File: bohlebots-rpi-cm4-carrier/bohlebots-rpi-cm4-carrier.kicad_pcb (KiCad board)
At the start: 2 copper layers, 28 parts, among them J1 SI-46001-F, J2 power_reference, J3 IO_Conn_02x05, J4 I2C_Conn_1x04, K1 Kicker, T1 Taster_LED, T2 Taster_LED, U1 Compute_Module_4_Connectors, U2 USB_Conn_01x05_Pin, X1 Miromatch

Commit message: Added esd protection TODO: find fitting tvs diode (tht) 2p, 4p
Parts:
- removed C1: 100n, Capacitor_THT:C_Radial_D5.0mm_H11.0mm_P2.00mm
- removed C2: 10u, Capacitor_THT:C_Radial_D5.0mm_H11.0mm_P2.00mm
- removed D1: LED, LED_THT:LED_D5.0mm_FlatTop
- removed D36V28FX1: 5V, bohlebots:D36V28FX
- removed D36V28FX2: 3.3V, bohlebots:D36V28FX
- removed ESCON1, ESCON2, ESCON3, ESCON4: 24_2, bohlebots:ESCOM_24_2
- removed H1: Pinhead_1x04V, bohlebots:PinHeader_1x04_P2.54mm_Vertical
- removed J1: SI-46001-F, SI_46001_F:CONN_46001-F_BEL
- removed J2: power_reference, Connector_PinHeader_2.54mm:PinHeader_1x02_P2.54mm_Vertical
- removed J3: IO_Conn_02x05, Connector_PinHeader_2.54mm:PinHeader_2x06_P2.54mm_Vertical
- removed J4: I2C_Conn_1x04, Connector_PinHeader_2.54mm:PinHeader_1x04_P2.54mm_Vertical
- removed JP1, JP2, JP3, JP4: B8B-PH-K, bohlebots:B8B-PH-K
- removed K1: Kicker, bohlebots:KICKER
- removed R1, R2, R3: 10k, Resistor_THT:R_Axial_DIN0207_L6.3mm_D2.5mm_P7.62mm_Horizontal
- removed R4: 1k, Resistor_THT:R_Axial_DIN0207_L6.3mm_D2.5mm_P7.62mm_Horizontal
- removed T1, T2: Taster_LED, bohlebots:TASTER_LED
- removed U1: Compute_Module_4_Connectors, RPi_Compute_Module_4:Raspberry-Pi-4-Compute-Module
- removed U2: USB_Conn_01x05_Pin, Connector_PinHeader_2.54mm:PinHeader_1x04_P2.54mm_Vertical
- removed X1: Miromatch, bohlebots:MICROMATCH-4

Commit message: Started routing.
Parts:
- added C1: 100n, Capacitor_THT:C_Radial_D5.0mm_H11.0mm_P2.00mm, F.Cu at (99.1, 31.6)
- added C2: 10u, Capacitor_THT:C_Radial_D5.0mm_H11.0mm_P2.00mm, F.Cu at (99.1, 38.1)
- added D1: LED, LED_THT:LED_D5.0mm_FlatTop, F.Cu at (83.8, 53.3)
- added D36V28FX1: 5V, bohlebots:D36V28FX, F.Cu at (238.9, 40.0)
- added D36V28FX2: 3.3V, bohlebots:D36V28FX, F.Cu at (259.8, 40.0)
- added ESCON1: 24_2, bohlebots:ESCOM_24_2, F.Cu at (36.6, 87.5)
- added ESCON2: 24_2, bohlebots:ESCOM_24_2, F.Cu at (36.6, 115.3)
- added ESCON3: 24_2, bohlebots:ESCOM_24_2, F.Cu at (36.6, 143.1)
- added ESCON4: 24_2, bohlebots:ESCOM_24_2, F.Cu at (36.6, 170.9)
- added H1: Pinhead_1x04V, bohlebots:PinHeader_1x04_P2.54mm_Vertical, F.Cu at (58.4, 30.3)
- added J1: SI-46001-F, SI_46001_F:CONN_46001-F_BEL, F.Cu at (241.3, 106.7)
- added J2: power_reference, Connector_PinHeader_2.54mm:PinHeader_1x02_P2.54mm_Vertical, F.Cu at (238.8, 81.3)
- added J3: IO_Conn_02x05, Connector_PinHeader_2.54mm:PinHeader_2x06_P2.54mm_Vertical, F.Cu at (251.5, 78.7)
- added J4: I2C_Conn_1x04, Connector_PinHeader_2.54mm:PinHeader_1x04_P2.54mm_Vertical, F.Cu at (63.5, 30.3)
- added JP1: B8B-PH-K, bohlebots:B8B-PH-K, F.Cu at (103.7, 154.9)
- added JP2: B8B-PH-K, bohlebots:B8B-PH-K, F.Cu at (124.9, 154.9)
- added JP3: B8B-PH-K, bohlebots:B8B-PH-K, F.Cu at (103.7, 165.1)
- added JP4: B8B-PH-K, bohlebots:B8B-PH-K, F.Cu at (124.5, 165.1)
- added K1: Kicker, bohlebots:KICKER, F.Cu at (63.5, 182.9)
- added R1: 10k, Resistor_THT:R_Axial_DIN0207_L6.3mm_D2.5mm_P7.62mm_Horizontal, F.Cu at (80.7, 27.9)
- added R2: 10k, Resistor_THT:R_Axial_DIN0207_L6.3mm_D2.5mm_P7.62mm_Horizontal, F.Cu at (80.7, 31.9)
- added R3: 10k, Resistor_THT:R_Axial_DIN0207_L6.3mm_D2.5mm_P7.62mm_Horizontal, F.Cu at (80.7, 36.0)
- added R4: 1k, Resistor_THT:R_Axial_DIN0207_L6.3mm_D2.5mm_P7.62mm_Horizontal, F.Cu at (80.7, 40.0)
- added T1: Taster_LED, bohlebots:TASTER_LED, F.Cu at (35.5, 36.2)
- added T2: Taster_LED, bohlebots:TASTER_LED, F.Cu at (35.6, 55.9)
- added U1: Compute_Module_4_Connectors, RPi_Compute_Module_4:Raspberry-Pi-4-Compute-Module, F.Cu at (138.0, 71.6)
- added U2: USB_Conn_01x05_Pin, Connector_PinHeader_2.54mm:PinHeader_1x04_P2.54mm_Vertical, F.Cu at (68.6, 30.3)
- added U3: DT1446-04SO-7, bohlebots-rpi-cm4-carrier:SOT26, F.Cu at (65.1, 49.6)
- added U5: DT1446-04SO-7, bohlebots-rpi-cm4-carrier:SOT26, F.Cu at (63.5, 58.4)
- added X1: Miromatch, bohlebots:MICROMATCH-4, F.Cu at (109.2, 27.9)

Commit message: PCB Layout Update.
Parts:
- moved J4 199.5 mm to (251.0, -37.8)
- moved R1 199.1 mm to (35.5, 221.8)
- moved R4 186.5 mm to (197.8, 185.2)
- moved T1 175.1 mm to (185.0, -55.0)
- moved R2 171.9 mm to (248.4, -5.80)
- moved R3 171.6 mm to (248.4, -0.74)
- moved U2 171.4 mm to (229.1, 90.4), turned to -90 degrees
- moved J2 169.3 mm to (76.0, 34.5)
- moved D1 168.7 mm to (200.2, 175.5)
- moved U5 164.1 mm to (225.2, 86.5), turned to 90 degrees
- moved T2 160.0 mm to (150.5, -55.5)
- moved U3 148.9 mm to (210.7, 18.6), turned to 180 degrees
- moved X1 148.7 mm to (250.7, -17.8)
- moved D36V28FX1 120.6 mm to (355.5, 70.9)
- moved D36V28FX2 117.0 mm to (355.5, 107.4)
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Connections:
- U5 pad 1: Net-(U5-D1-) -> /USB_N
- U5 pad 3: /USB_P -> Net-(U5-D2-)
- U5 pad 4: /USB_N -> Net-(U5-D2+)

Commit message: Updated pcb layout.
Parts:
- moved D1 251.1 mm to (357.9, -19.9)
- moved R4 251.1 mm to (355.4, -10.3)
- moved J3 225.8 mm to (342.7, -23.5)
- moved U2 128.4 mm to (311.1, -8.42)
- moved U1 128.4 mm to (291.2, -36.9)
- moved U5 128.4 mm to (307.2, -12.4)
- moved C1 128.4 mm to (286.2, -79.7)
- moved J1 128.4 mm to (288.4, -72.8)
- moved U3 128.4 mm to (292.7, -80.2)
- moved H1 118.8 mm to (-60.4, 29.7)
- moved K1 115.9 mm to (-93.1, 217.1)
- moved C2 115.9 mm to (-50.9, 32.4)
- moved ESCON1 115.9 mm to (-79.9, 84.9)
- moved ESCON2 115.9 mm to (-80.0, 113.7)
- moved ESCON3 115.9 mm to (-80.0, 141.5)
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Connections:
- U1 pad 78: unconnected-(U1A-GPIO_VREF-Pad78) -> Net-(U1A-GPIO_VREF)
- U1 pad 84: Net-(U1A-CM4_3.3V_Out-Pad84) -> Net-(U1A-GPIO_VREF)
- U1 pad 86: Net-(U1A-CM4_3.3V_Out-Pad84) -> Net-(U1A-GPIO_VREF)
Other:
- board text added: "Chassie Rand"
- board text added: "Spiegel Zone"

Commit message: IC placement done.
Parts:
- removed H1: Pinhead_1x04V, bohlebots:PinHeader_1x04_P2.54mm_Vertical
- added J5: pwr_connector, Connector_PinHeader_2.54mm:PinHeader_1x03_P2.54mm_Vertical, F.Cu at (48.5, 102.5)
- added J6: pwr_connector, Connector_PinHeader_2.54mm:PinHeader_1x03_P2.54mm_Vertical, F.Cu at (163.5, 107.5)
- added Luxonis OAK-FFP 4P: Luxonis_OAK-FFC-4P_Foothold, bohlebots-rpi-cm4-carrier:Luxonis_OAK-FFC-4P_Foothold, F.Cu at (106.0, 105.0)
- moved D36V28FX2 348.5 mm to (88.5, 117.4)
- moved D36V28FX1 318.7 mm to (118.5, 117.4)
- moved U2 272.0 mm to (65.5, 108.5), turned to 180 degrees
- moved J3 271.4 mm to (80.0, 44.4)
- moved U5 264.6 mm to (70.0, 105.0), turned to 0 degrees
- moved U3 249.1 mm to (129.0, 107.5)
- moved ESCON3 239.7 mm to (150.0, 74.0), turned to 135 degrees
- moved J1 236.4 mm to (137.0, 108.8), turned to 90 degrees
- moved C1 232.6 mm to (131.0, 93.5), turned to 180 degrees
- moved ESCON2 231.0 mm to (150.0, 136.0), turned to 45 degrees
- moved D1 230.7 mm to (138.0, 50.0), turned to 180 degrees
- moved R4 228.9 mm to (136.8, 57.5), turned to 180 degrees
- moved U1 212.6 mm to (106.0, 67.5), turned to 180 degrees
- moved K1 206.3 mm to (91.6, 125.2), turned to -90 degrees
- moved JP3 205.2 mm to (143.0, 68.0), turned to 135 degrees
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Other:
- board text added: "Ballschale"

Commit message: V01 finished.
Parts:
- added G***: LOGO, bohlebots:logo_klein, F.Cu at (126.4, 129.1)
- added G***: LOGO, RPi_Compute_Module_4:logo, F.Cu at (98.9, 75.7)
- added REF**: MountingHole_4.3mm_M4, MountingHole:MountingHole_4.3mm_M4, F.Cu at (167.5, 88.5)
- added REF**: BohlebotsBigBrother_Logo, bohlebots-rpi-cm4-carrier:BohlebotsBigBrother_Logo, F.Cu at (71.5, 96.5)
- added REF**: MountingHole_4.3mm_M4, MountingHole:MountingHole_4.3mm_M4, F.Cu at (43.5, 122.5)
- added REF**: MountingHole_4.3mm_M4, MountingHole:MountingHole_4.3mm_M4, F.Cu at (43.5, 88.5)
- added REFe: MountingHole_4.3mm_M4, MountingHole:MountingHole_4.3mm_M4, F.Cu at (167.5, 122.5)
- added U4: DT1446-04SO-7, bohlebots-rpi-cm4-carrier:SOT26, F.Cu at (130.0, 104.2)
- moved U2 8.44 mm to (60.5, 101.7), turned to 0 degrees
- moved U5 6.05 mm to (64.0, 105.5), turned to 90 degrees
- moved X1 5.44 mm to (77.7, 104.9)
- moved R3 3.35 mm to (93.3, 110.5)
- moved R2 2.87 mm to (93.3, 114.5)
- moved D36V28FX1 2.55 mm to (116.0, 117.9)
- moved D36V28FX2 1.58 mm to (90.0, 117.9)
- moved U3 1.12 mm to (130.0, 108.0), turned to 90 degrees
- moved C1 0.71 mm to (130.5, 94.0)
- moved C2 0.71 mm to (52.5, 103.0)
- moved D1 0.71 mm to (137.5, 50.5)
- moved ESCON1 0.71 mm to (61.5, 136.5)
- moved ESCON2 0.71 mm to (149.5, 136.5)
- moved ESCON3 0.71 mm to (149.5, 74.5)
- moved ESCON4 0.71 mm to (61.5, 74.5)
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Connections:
- ESCON2 pad P15: /DIR1 -> /DIR2
- ESCON2 pad P17: /PWM1 -> /PWM2
- ESCON3 pad P15: /DIR1 -> /DIR3
- ESCON3 pad P17: /PWM1 -> /PWM3
- ESCON4 pad P15: /DIR1 -> /DIR4
- ESCON4 pad P17: /PWM1 -> /PWM4
- T1 pad 1: /3.3v -> 3.3V
- T1 pad 8: /3.3v -> 3.3V
- T2 pad 1: /3.3v -> 3.3V
- T2 pad 8: /3.3v -> 3.3V
- U3 pad 1: /RD_N -> /TD_P
- U3 pad 4: /TD_P -> /TD_N
- U3 pad 6: /RD_P -> /TD_P
- U5 pad 1: /USB_N -> /USB_P
- U5 pad 3: Net-(U5-D2-) -> /USB_N
- U5 pad 4: Net-(U5-D2+) -> /USB_N
- X1 pad 1: /3.3v -> 3.3V
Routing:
- net /ENA: track 0.00 -> 375.8 mm, vias 0 -> 13
- net 3.3V: track 0.00 -> 277.7 mm, vias 0 -> 3
- net 16V: track 0.00 -> 275.4 mm
- net /SCL: track 0.00 -> 239.5 mm, vias 0 -> 6
- net /SDA: track 0.00 -> 237.1 mm, vias 0 -> 6
- net 5V: track 0.00 -> 206.2 mm, vias 0 -> 5
- net Net-(J5-GND): track 0.00 -> 173.6 mm
- net /PWM4: track 0.00 -> 128.2 mm, vias 0 -> 4
- net /DIR4: track 0.00 -> 123.6 mm, vias 0 -> 4
- net /DIR1: track 0.00 -> 118.5 mm, vias 0 -> 4
- net /PWM1: track 0.00 -> 118.1 mm, vias 0 -> 6
- net /DIR2: track 0.00 -> 98.8 mm, vias 0 -> 2
- net /PWM2: track 0.00 -> 95.5 mm, vias 0 -> 4
- net /KICK: track 0.00 -> 89.7 mm, vias 0 -> 6
- net /UART0_TXD: track 0.00 -> 69.5 mm, vias 0 -> 2
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- added copper zone on B.Cu, net GND
- added copper zone on F.Cu, net GND
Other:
- board outline added: 132 x 132 mm
- board text added: "Rpi CM4 Carrier BohleBots BigBrother"

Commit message: V01.2 Update.
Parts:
- added U6: DT1446-04SO-7, bohlebots-rpi-cm4-carrier:SOT26, F.Cu at (71.9, 159.3)
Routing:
- net 3.3V: track 277.7 -> 289.7 mm
- net /SCL: track 239.5 -> 247.1 mm
- net /SDA: track 237.1 -> 244.7 mm
- net /SPI0_MISO: track 60.0 -> 61.0 mm
- net GND: vias 42 -> 43

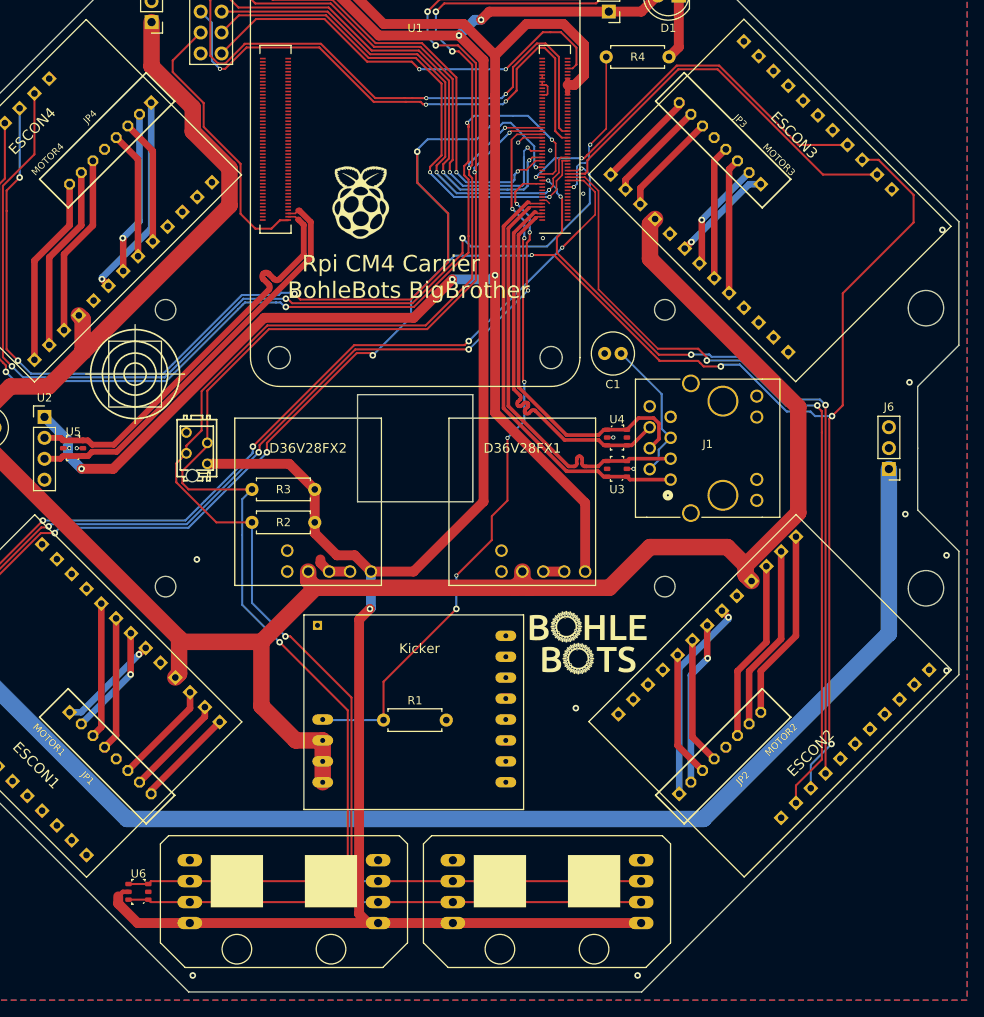
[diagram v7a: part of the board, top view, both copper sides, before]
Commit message: Added some vias.
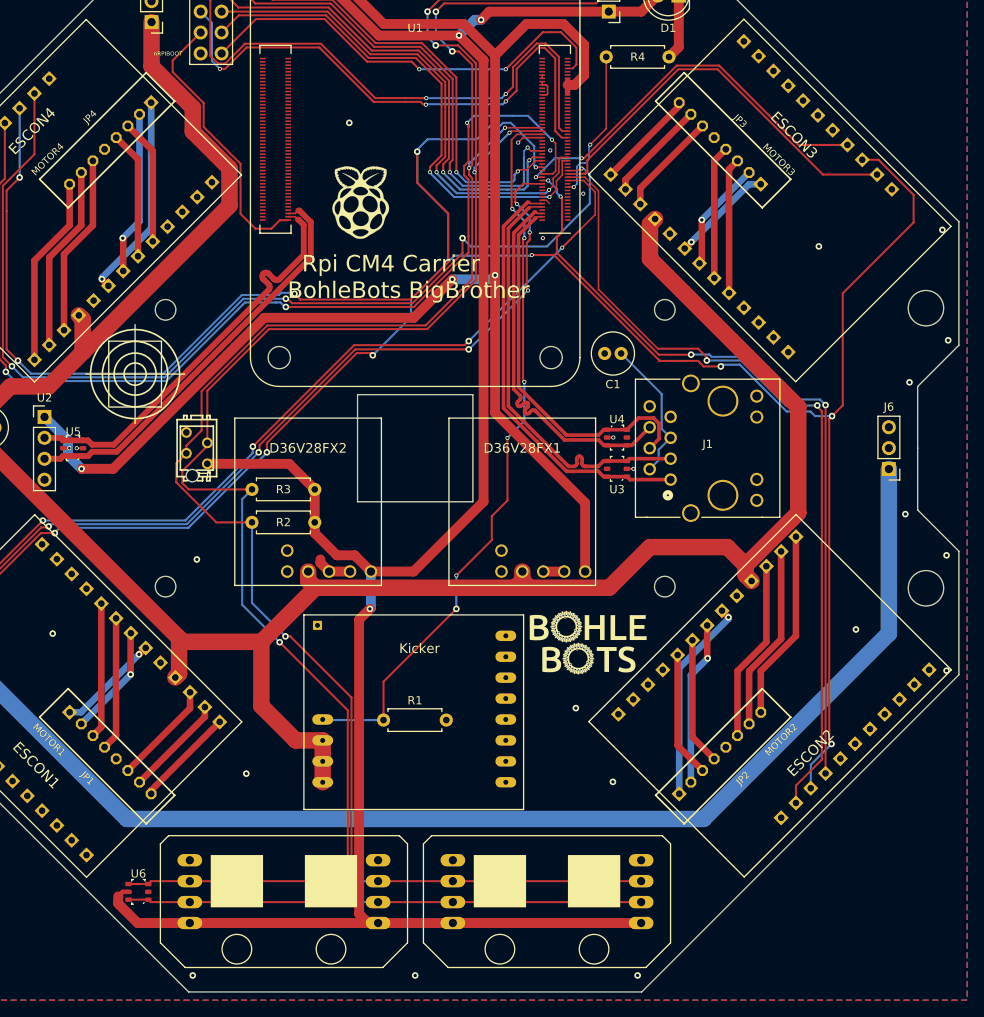
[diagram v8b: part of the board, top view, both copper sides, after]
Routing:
- net GND: vias 43 -> 51
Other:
- board text added: "nRPIBOOT"
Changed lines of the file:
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@@
     (effects (font (size 2 2) (thickness 0.3)) (justify left bottom))
+  )
+  (gr_text "nRPIBOOT" (at 73.75 57.9) (layer "F.SilkS")
+    (effects (font (size 0.5 0.5) (thickness 0.075)) (justify left bottom))
   )
   (gr_text "Spiegel Zone" (at 59.5 77.5) (layer "User.1")
@@
   (via (at 112.5 50) (size 0.8) (drill 0.4) (layers "F.Cu" "B.Cu") (free) (net 2))
   (via (at 129.55 104.2) (size 0.5) (drill 0.3) (layers "F.Cu" "B.Cu") (net 2))
+  (via (at 129.5 146) (size 0.8) (drill 0.4) (layers "F.Cu" "B.Cu") (free) (net 2))
   (via (at 106.5 50) (size 0.8) (drill 0.4) (layers "F.Cu" "B.Cu") (free) (net 2))
   (via (at 115.5 46) (size 0.8) (drill 0.4) (layers "F.Cu" "B.Cu") (free) (net 2))
@@
   (via (at 64.42 105.5) (size 0.5) (drill 0.3) (layers "F.Cu" "B.Cu") (net 2))
   (via (at 118 68.4) (size 0.5) (drill 0.3) (layers "F.Cu" "B.Cu") (net 2))
+  (via (at 61.5 128) (size 0.8) (drill 0.4) (layers "F.Cu" "B.Cu") (free) (net 2))
   (via (at 170 118.5) (size 0.8) (drill 0.4) (layers "F.Cu" "B.Cu") (free) (net 2))
   (via (at 41 79) (size 0.8) (drill 0.4) (layers "F.Cu" "B.Cu") (free) (net 2))
   (via (at 132 108) (size 0.5) (drill 0.3) (layers "F.Cu" "B.Cu") (net 2))
   (via (at 165.5 97.5) (size 0.8) (drill 0.4) (layers "F.Cu" "B.Cu") (free) (net 2))
+  (via (at 159 127.5) (size 0.8) (drill 0.4) (layers "F.Cu" "B.Cu") (free) (net 2))
+  (via (at 97.5 66) (size 0.8) (drill 0.4) (layers "F.Cu" "B.Cu") (free) (net 2))
   (via (at 114.5 42.5) (size 0.8) (drill 0.4) (layers "F.Cu" "B.Cu") (free) (net 2))
   (via (at 104.5 50) (size 0.8) (drill 0.4) (layers "F.Cu" "B.Cu") (free) (net 2))
@@
   (via (at 103.5 44) (size 0.8) (drill 0.4) (layers "F.Cu" "B.Cu") (free) (net 2))
   (via (at 165 113.5) (size 0.8) (drill 0.4) (layers "F.Cu" "B.Cu") (free) (net 2))
+  (via (at 85 145) (size 0.8) (drill 0.4) (layers "F.Cu" "B.Cu") (free) (net 2))
   (via (at 41 119) (size 0.8) (drill 0.4) (layers "F.Cu" "B.Cu") (free) (net 2))
   (via (at 108.5 50) (size 0.8) (drill 0.4) (layers "F.Cu" "B.Cu") (free) (net 2))
@@
   (via (at 86.1 159.3) (size 0.8) (drill 0.4) (layers "F.Cu" "B.Cu") (free) (net 2))
   (via (at 132.5 169.5) (size 0.8) (drill 0.4) (layers "F.Cu" "B.Cu") (free) (net 2))
+  (via (at 105.5 169.5) (size 0.8) (drill 0.4) (layers "F.Cu" "B.Cu") (free) (net 2))
   (via (at 115.5 48) (size 0.8) (drill 0.4) (layers "F.Cu" "B.Cu") (free) (net 2))
   (via (at 108.5 42.5) (size 0.8) (drill 0.4) (layers "F.Cu" "B.Cu") (free) (net 2))
@@
   (via (at 106.5 42.5) (size 0.8) (drill 0.4) (layers "F.Cu" "B.Cu") (free) (net 2))
   (via (at 110.5 42.5) (size 0.8) (drill 0.4) (layers "F.Cu" "B.Cu") (free) (net 2))
+  (via (at 170.2 92.4) (size 0.8) (drill 0.4) (layers "F.Cu" "B.Cu") (free) (net 2))
   (via (at 169.5 79) (size 0.8) (drill 0.4) (layers "F.Cu" "B.Cu") (free) (net 2))
+  (via (at 154.5 81) (size 0.8) (drill 0.4) (layers "F.Cu" "B.Cu") (free) (net 2))
   (via (at 46 97.5) (size 0.8) (drill 0.4) (layers "F.Cu" "B.Cu") (free) (net 2))
   (via (at 114.5 50) (size 0.8) (drill 0.4) (layers "F.Cu" "B.Cu") (free) (net 2))
